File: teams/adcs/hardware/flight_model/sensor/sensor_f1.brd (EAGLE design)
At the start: 94 x 94 mm, 73 parts, among them U1 LT1761-X, U2 LT1761-X, U3 OEM719, U4 LTC3624

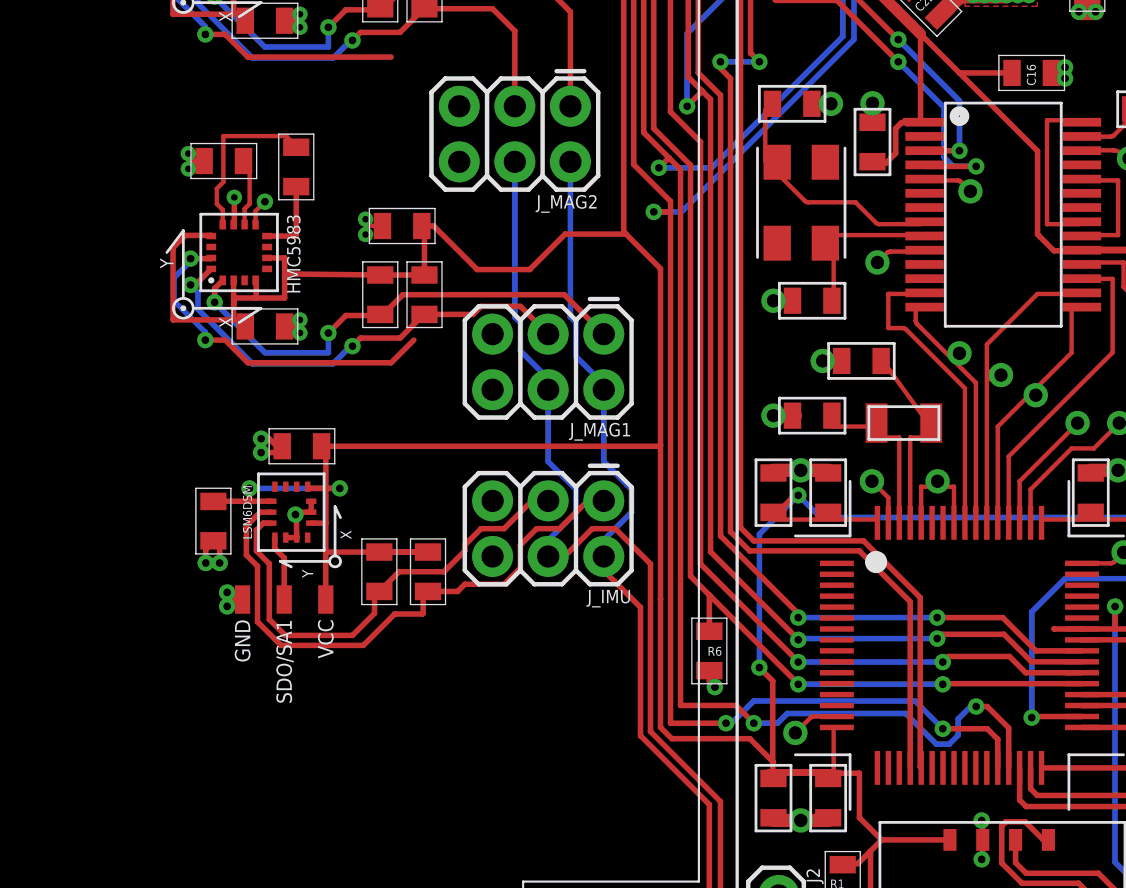
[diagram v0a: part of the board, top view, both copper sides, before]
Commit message: ADCS/Sensor: Rename board files and reconnect second magnetometer ti I2C bus 2
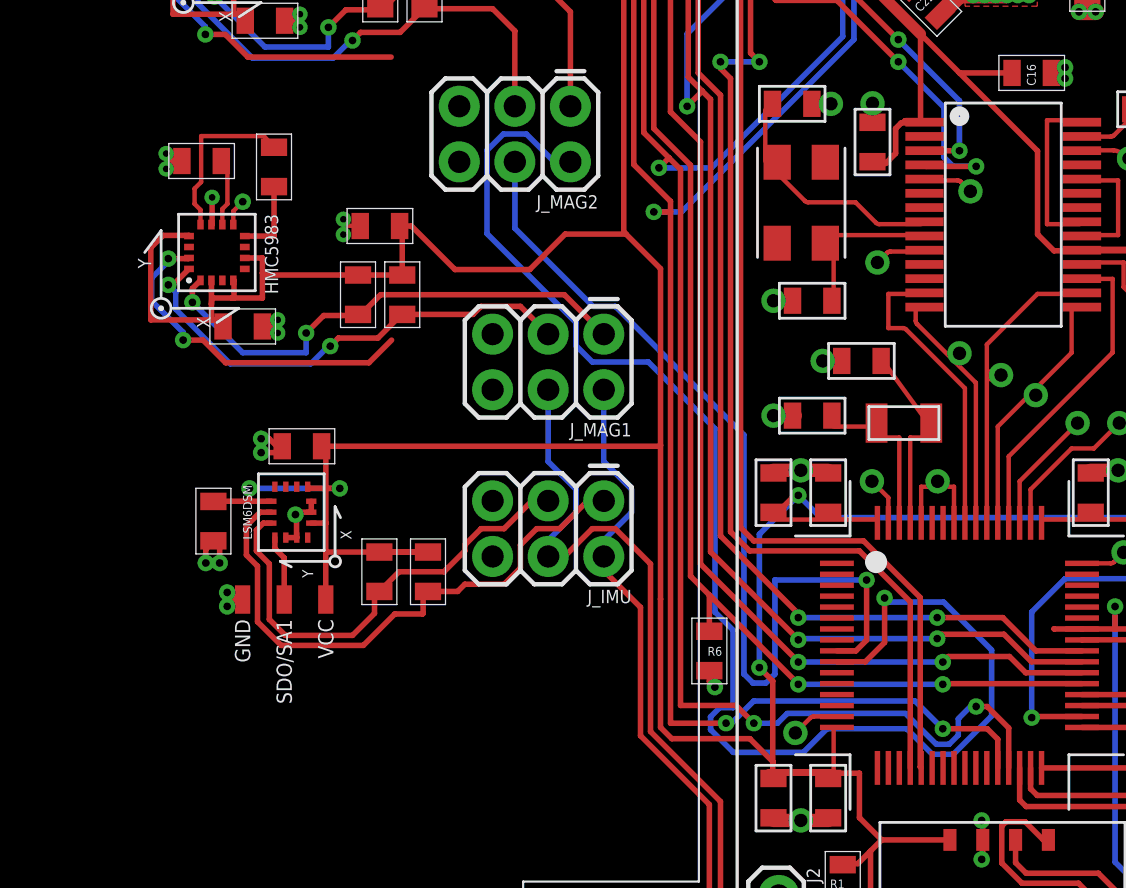
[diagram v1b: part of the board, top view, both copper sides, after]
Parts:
- moved C30 1.02 mm to (41.3, 45.7)
- moved C32 1.02 mm to (39.9, 38.5)
- moved R12 1.02 mm to (47.2, 39.9)
- moved C29 1.02 mm to (38.0, 46.0)
- moved C31 1.02 mm to (46.2, 43.0)
- moved R11 1.02 mm to (45.2, 39.9)
- moved U$6 1.02 mm to (38.7, 41.8)
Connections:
- new net I2C_SCL_2: BLK1.P7.1_I2C-SCL-2, J_MAG2.2
- new net I2C_SDA_2: BLK1.P7.0_I2C-SDA-2, J_MAG2.4
- net I2C_SCL: no longer J_MAG2.2
- net I2C_SDA: no longer J_MAG2.4
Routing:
- net I2C_SCL_2: track 0.00 -> 66.5 mm, vias 0 -> 1
- net I2C_SDA_2: track 0.00 -> 42.9 mm, vias 0 -> 1
- net I2C_SCL: track 132.5 -> 121.5 mm
- net I2C_SDA: track 128.6 -> 117.6 mm
- net LDO_3V3: track 371.6 -> 372.6 mm
- net MAG1_SDA: track 21.1 -> 22.2 mm
- net MAG1_SCL: track 22.3 -> 23.3 mm

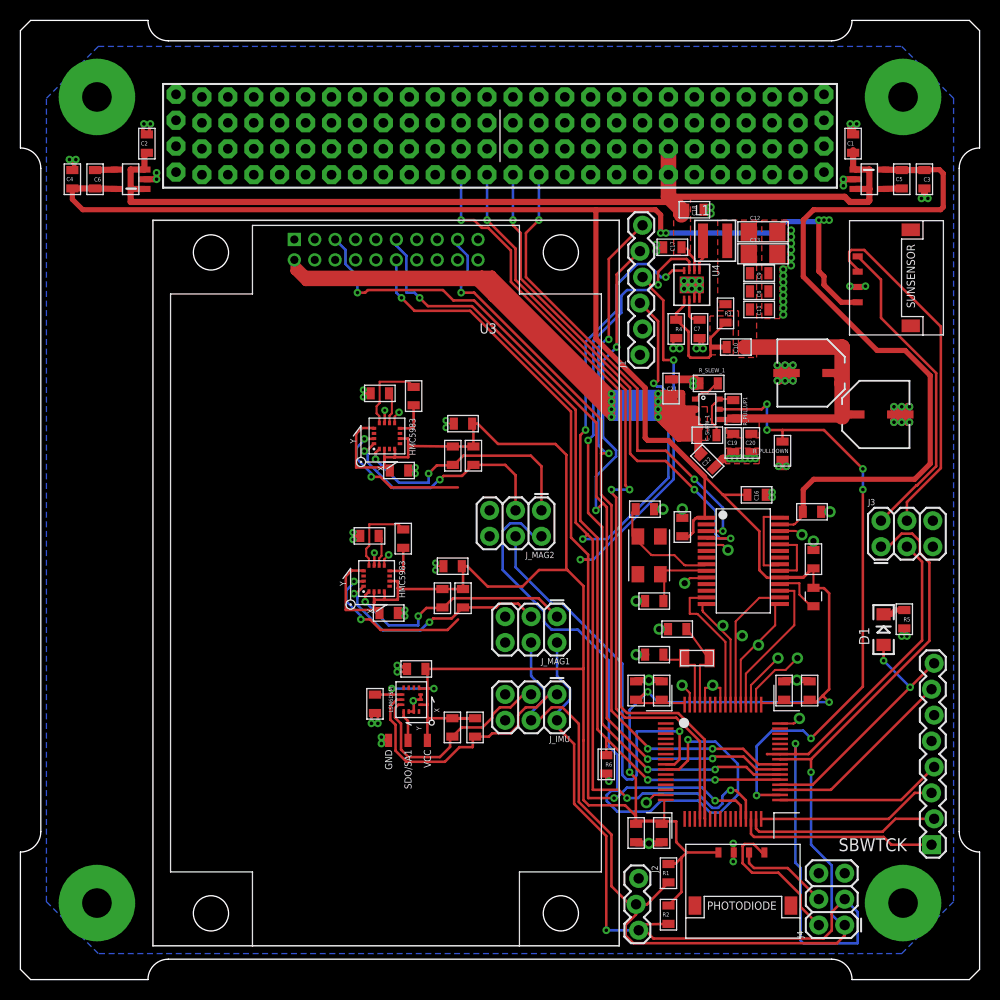
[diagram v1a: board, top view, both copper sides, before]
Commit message: ADCS/Sensor: Rotate IMU and fix layers for silkscreen
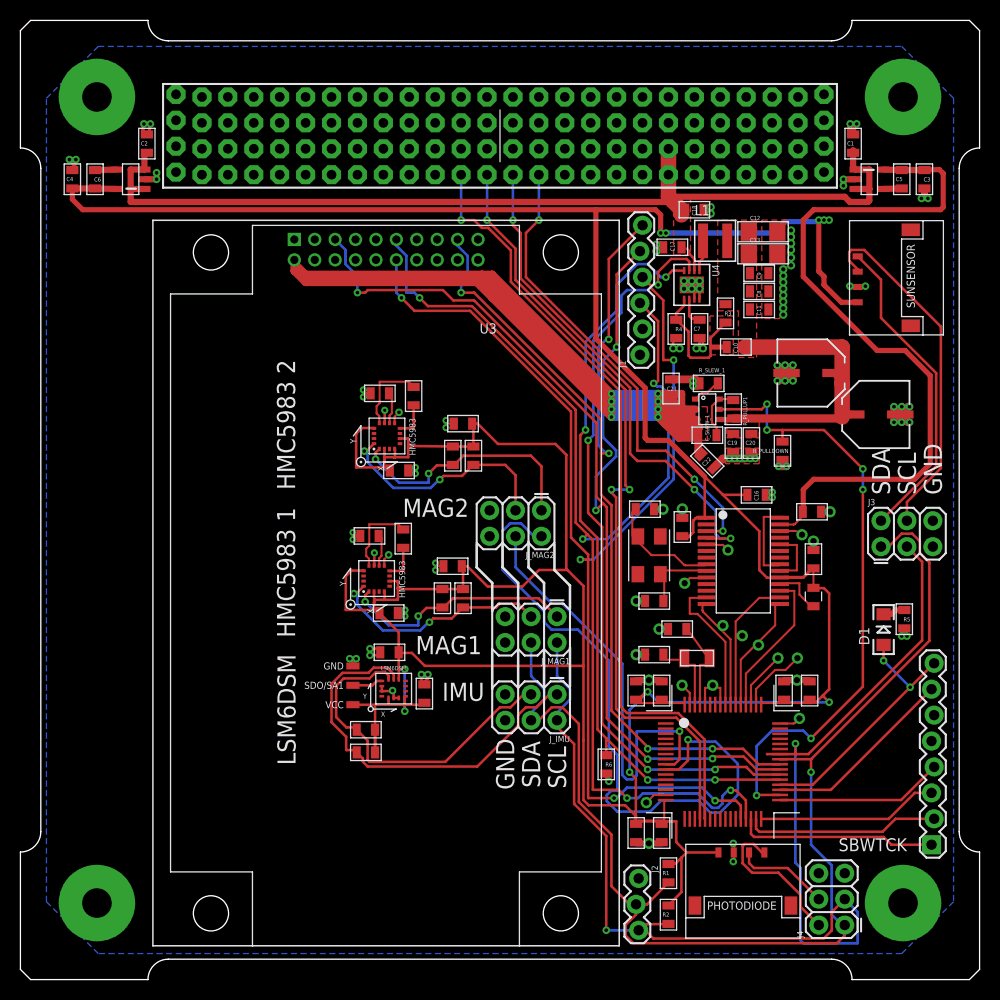
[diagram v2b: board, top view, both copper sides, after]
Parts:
- moved R10 11.0 mm to (37.7, 24.8), turned to 180 degrees
- moved R9 8.48 mm to (37.7, 27.0), turned to 180 degrees
- moved SDO/SA1 7.63 mm to (36.4, 31.4), turned to 180 degrees
- moved C25 5.25 mm to (40.0, 34.6), turned to 180 degrees
- moved C26 2.55 mm to (43.4, 30.6), turned to 270 degrees
- moved U$5 2.04 mm to (40.4, 31.0), turned to 0 degrees
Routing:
- net MAG1_DRDY: track 16.0 -> 0.00 mm, vias 2 -> 0
- net MAG2_DRDY: track 14.5 -> 0.00 mm, vias 2 -> 0
- net IMU_SCL: track 26.1 -> 39.3 mm
- net IMU_SDA: track 21.6 -> 34.3 mm
- net LDO_3V3: track 372.6 -> 380.4 mm

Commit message: Flight merge (#230)
Merge of the flight code into master
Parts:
- R1, R2: value 2.2k -> DNP
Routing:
- net MAG2_SDA: vias 2 -> 3
- net MAG1_SDA: vias 2 -> 3
- net LDO_3V3: vias 10 -> 11
- net I2C_SDA: vias 1 -> 2
- net GPS_POSITION_VALID: vias 5 -> 6
- net CANH: vias 3 -> 4
